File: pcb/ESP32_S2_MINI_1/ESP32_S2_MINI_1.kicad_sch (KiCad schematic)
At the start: 50 parts, among them J1 USB_C_Receptacle_USB2.0, J2 Conn_01x12_Female, J3 Conn_01x16_Female, J4 Conn_01x02_Female, J5 STEMMA, Q1 DMG3415u, U1 AP2112K-3.3, U2 ESP32-S2-MINI-1, U3 LTR-329ALS-01, U4 MT8691AT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

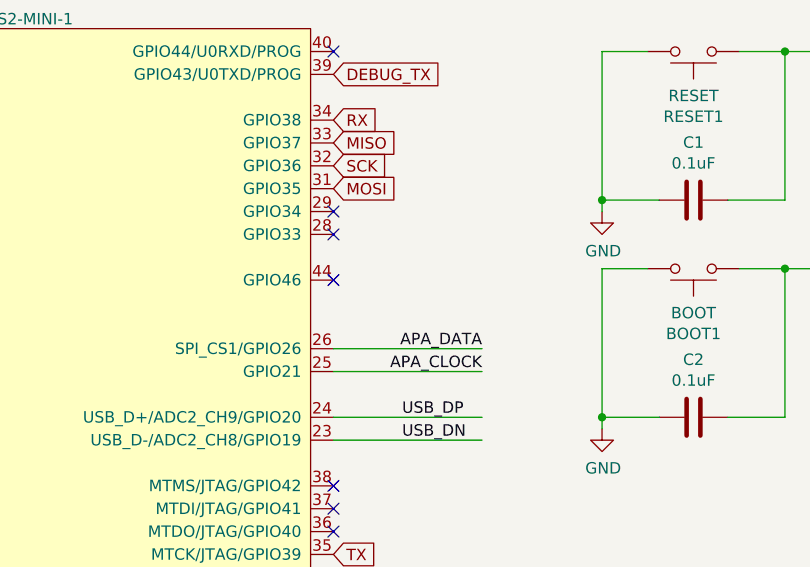
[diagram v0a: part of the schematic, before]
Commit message: Version 1.1, see Errata for fixes
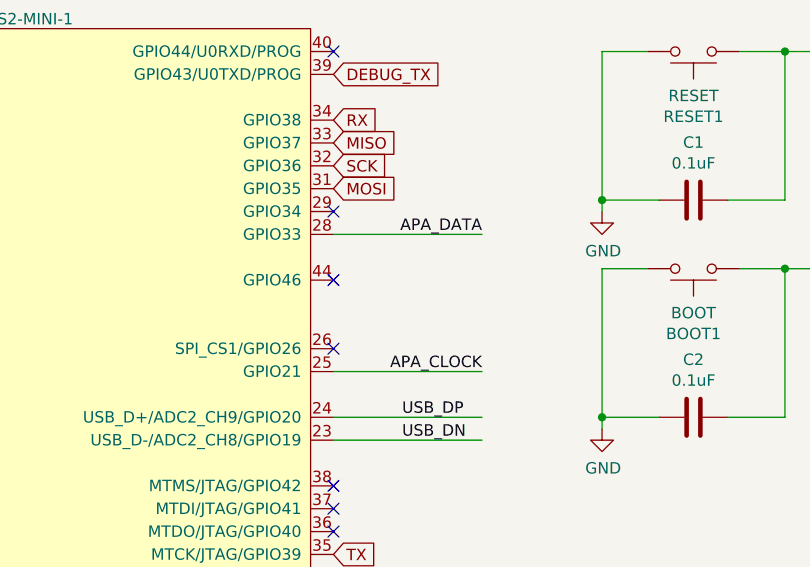
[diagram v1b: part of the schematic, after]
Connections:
- net APA_DATA: now also U2.28 (GPIO33); no longer U2.26 (SPI_CS1/GPIO26)
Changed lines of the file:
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@@
   (no_connect (at 45.085 172.085))
   (no_connect (at 37.465 29.845))
-  (no_connect (at 109.855 40.005))
+  (no_connect (at 109.855 52.705))
   (no_connect (at 264.795 145.415))
   (no_connect (at 264.795 147.955))
@@
     (stroke (width 0) (type default) (color 0 0 0 0))
   )
-  (wire (pts (xy 126.365 52.705) (xy 109.855 52.705))
+  (wire (pts (xy 126.365 40.005) (xy 109.855 40.005))
     (stroke (width 0) (type default) (color 0 0 0 0))
   )
@@
     (effects (font (size 1.27 1.27)) (justify left bottom))
   )
-  (label "APA_DATA" (at 126.365 52.705 180)
+  (label "APA_DATA" (at 126.365 40.005 180)
     (effects (font (size 1.27 1.27)) (justify right bottom))
   )

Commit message: S3 version
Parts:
- D3: value APA102-2020 -> (none); footprint LED_SMD:LED-APA102-2020 -> (none); MFGR (none) -> Shenzhen LED Color Co.,LTD; MPN (none) -> LC8822-2020-6
- D4, D6: value MSK4005 -> (none); footprint Diode_SMD:D_SOD-523 -> (none); MFGR (none) -> Shikues
- J1: value USB_C_Receptacle_USB2.0 -> (none); footprint USB-C-Power-tester:TYPE-C-31-M-12 -> (none); MFGR (none) -> Korean Hroparts Elec; MPN (none) -> TYPE-C-31-M-12
- Q1: value DMG3415u -> (none); footprint Package_TO_SOT_SMD:SOT-23 -> (none); MFGR (none) -> Diodes Incorporated; MPN (none) -> DMG3415U-7
- U1, U7: value AP2112K-3.3 -> (none); footprint Package_TO_SOT_SMD:SOT-23-5 -> (none); MFGR (none) -> Diodes Incorporated; MPN (none) -> AP2112K-3.3TRG1
- U2: value ESP32-S2-MINI-1 -> (none); footprint Espressif:ESP32-S2-MINI-1 -> (none); MFGR (none) -> Espressif Systems; MPN (none) -> ESP32-S3-MINI-1-N8
- U3: value LTR-329ALS-01 -> (none); footprint ToyTronics:LTR-329ALS-01 -> (none); MFGR (none) -> Lite-On; MPN (none) -> LTR-329ALS-01
- U4: value MT8691AT -> (none); footprint Package_TO_SOT_SMD:SOT-23 -> (none); MFGR (none) -> Honeywell
- U5: value LIS3DH -> (none); footprint Package_LGA:LGA-16_3x3mm_P0.5mm_LayoutBorder3x5y -> (none); MFGR (none) -> ST; MPN (none) -> LIS3DH
- U6: value SHT31-DIS -> (none); footprint Sensor_Humidity:Sensirion_DFN-8-1EP_2.5x2.5mm_P0.5mm_EP1.1x1.7mm -> (none); MFGR (none) -> Sensiron; MPN (none) -> SHT31-DIS
- U8: value MCP73831-2-OT -> (none); footprint Package_TO_SOT_SMD:SOT-23-5 -> (none); MFGR (none) -> Microchip Technology; MPN (none) -> MCP73831T-4ADI/OT
